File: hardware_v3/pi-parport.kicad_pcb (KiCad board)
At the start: 2 copper layers, 65 x 56 mm, 15 parts, among them J1 CONN_01X02, J2 40HAT, J3 Conn_02x13_Odd_Even, U1 CAT24C32, U2 SN74LVC161284DLR

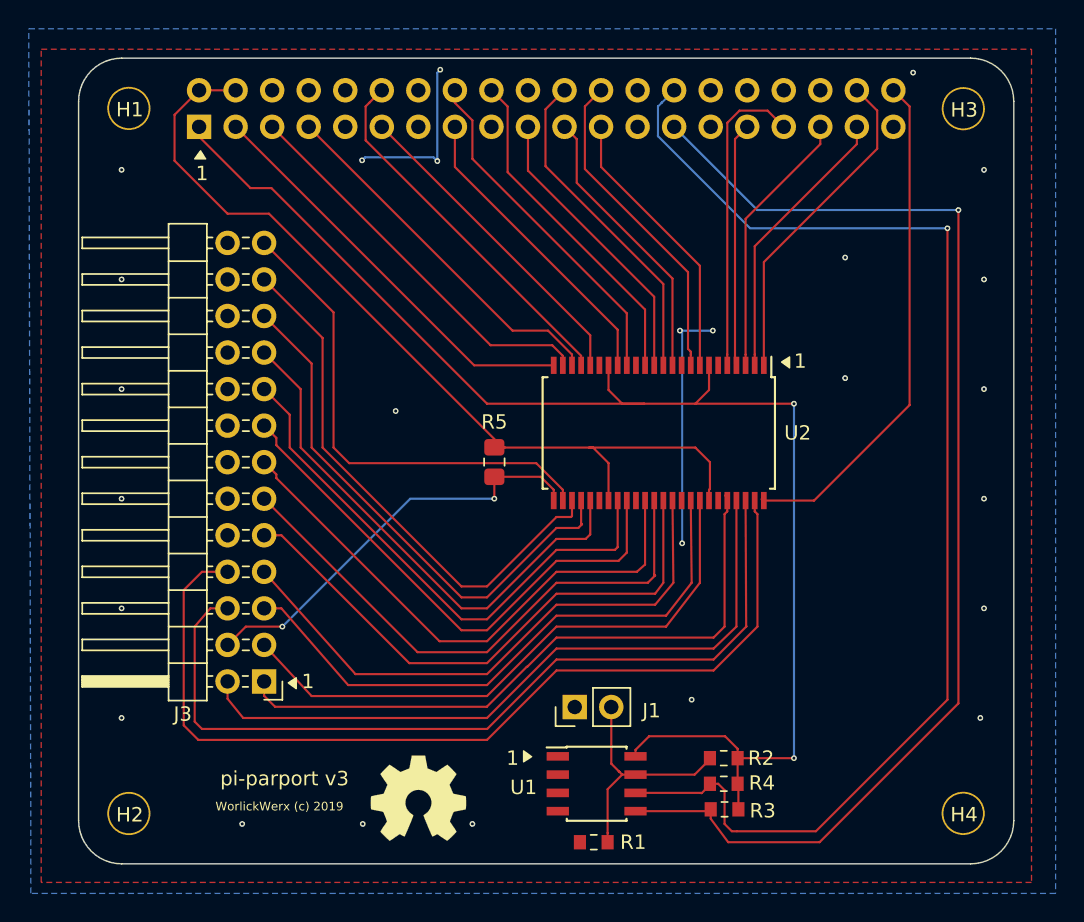
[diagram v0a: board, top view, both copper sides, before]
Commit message: hardware_v4: add bypass capacitors, reroute traces
Do not route trace under resistor R5.  Move U2 upward to facilitate
rerouting this trace without adding more vias.

Also make sure footprints between schematic and PCB are in sync.

Update BOM with new parts.

Hardware version needs to be bumped due to PCB changes.  Version numbers
in schematic and PCB source changed, new files will need to be generated
later.
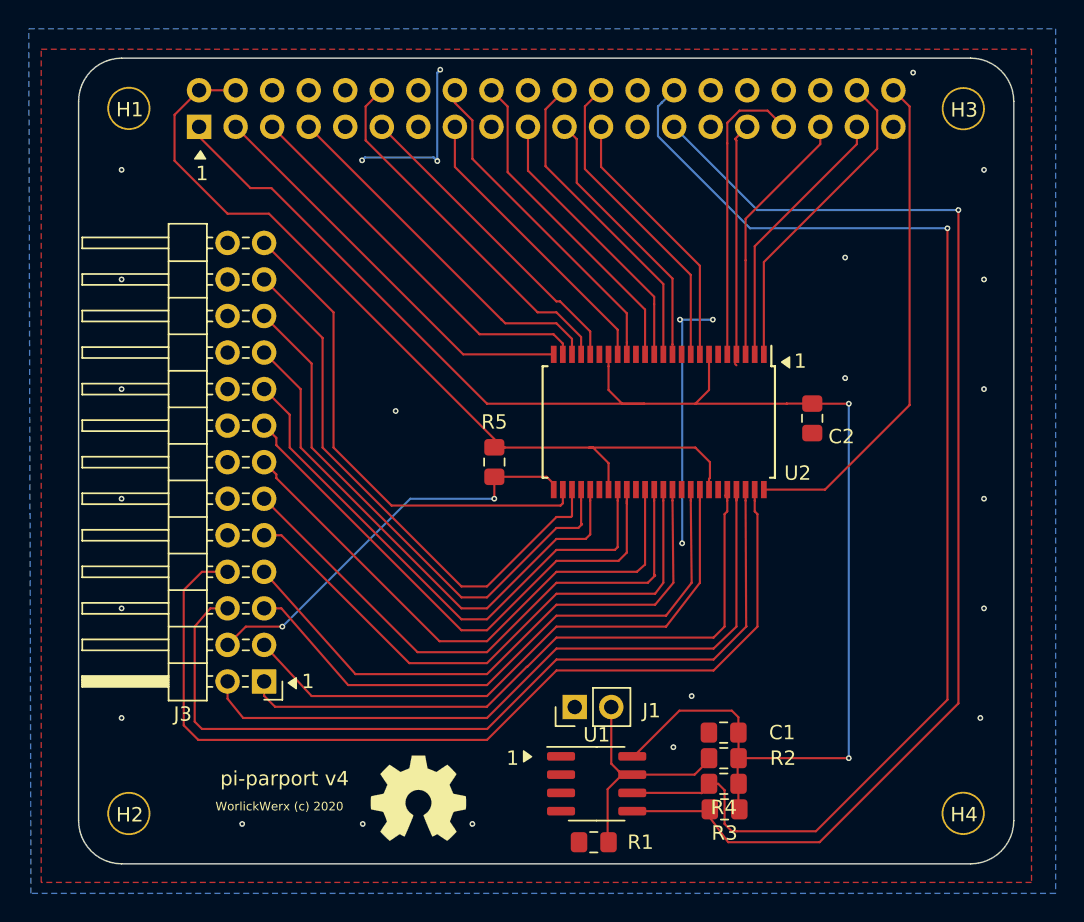
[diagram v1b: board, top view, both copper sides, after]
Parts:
- added C1: 100nF, Capacitor_SMD:C_0805_2012Metric_Pad1.15x1.40mm_HandSolder, F.Cu at (123.4, 107.7)
- added C2: 100nF, Capacitor_SMD:C_0805_2012Metric_Pad1.15x1.40mm_HandSolder, F.Cu at (129.5, 85.9)
- R1, R2, R3, R4: footprint Resistor_SMD:R_0603_1608Metric_Pad0.84x1.00mm_HandSolder -> Resistor_SMD:R_0805_2012Metric_Pad1.15x1.40mm_HandSolder
- U1: footprint Package_SOIC:SOIC-8_3.9x4.9mm_P1.27mm -> Package_SO:SOIC-8_3.9x4.9mm_P1.27mm
- moved U2 0.76 mm to (118.9, 86.1)
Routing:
- net +3V3: track 98.5 -> 110.2 mm
- net +5V: track 61.5 -> 59.9 mm
- net /DATA6: track 37.3 -> 38.2 mm
- net GND: track 29.0 -> 29.7 mm, vias 26 -> 27
- net /STATUS7: track 37.4 -> 38.2 mm
- net /STATUS6: track 36.9 -> 37.7 mm
- net /STATUS5: track 37.8 -> 38.6 mm
- net /GPIO9: track 19.7 -> 18.9 mm
- net /GPIO8: track 22.6 -> 21.9 mm
- net /GPIO26: track 19.5 -> 18.8 mm
- net /GPIO25: track 23.1 -> 22.3 mm
- net /GPIO24: track 23.5 -> 22.8 mm
- net /GPIO23: track 24.1 -> 23.3 mm
- net /GPIO22: track 21.3 -> 20.5 mm
- net /GPIO20: track 23.0 -> 22.2 mm
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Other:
- board text added: "WorlickWerx (c) 2020"
- board text added: "pi-parport v4"
- board text removed: "WorlickWerx (c) 2019"
- board text removed: "pi-parport v3"
